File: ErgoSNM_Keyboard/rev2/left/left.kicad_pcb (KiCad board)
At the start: 2 copper layers, 115.6 x 106.7 mm, 110 parts, among them J1 USB_C_Receptacle_USB2.0, J2 USB_C_Receptacle_USB2.0, J3 PJ-393_TRRS_8P, J4 Conn_01x08, SW1 BOOT, SW2 RESET, U1 RT9013-33GB, U2 SRV05-4, U3 W25Q128JVS, U4 RP2040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

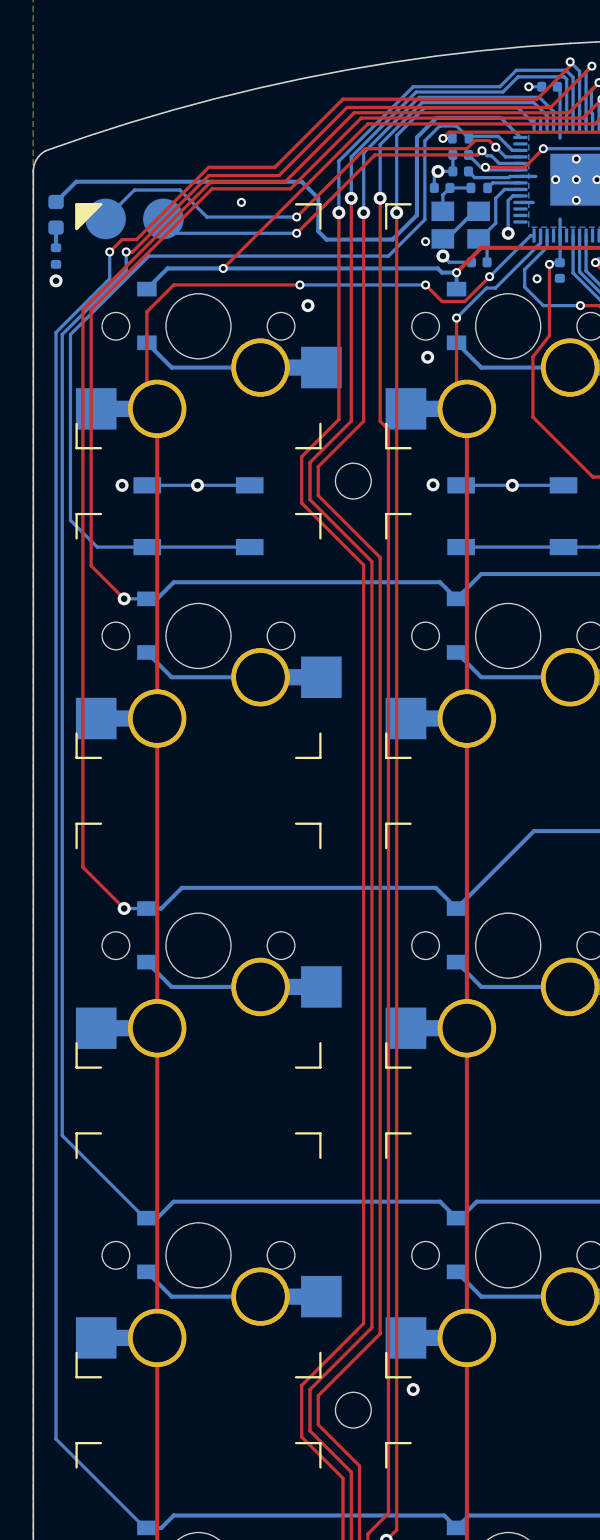
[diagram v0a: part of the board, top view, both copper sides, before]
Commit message: Add additional LED and upadrte LED position
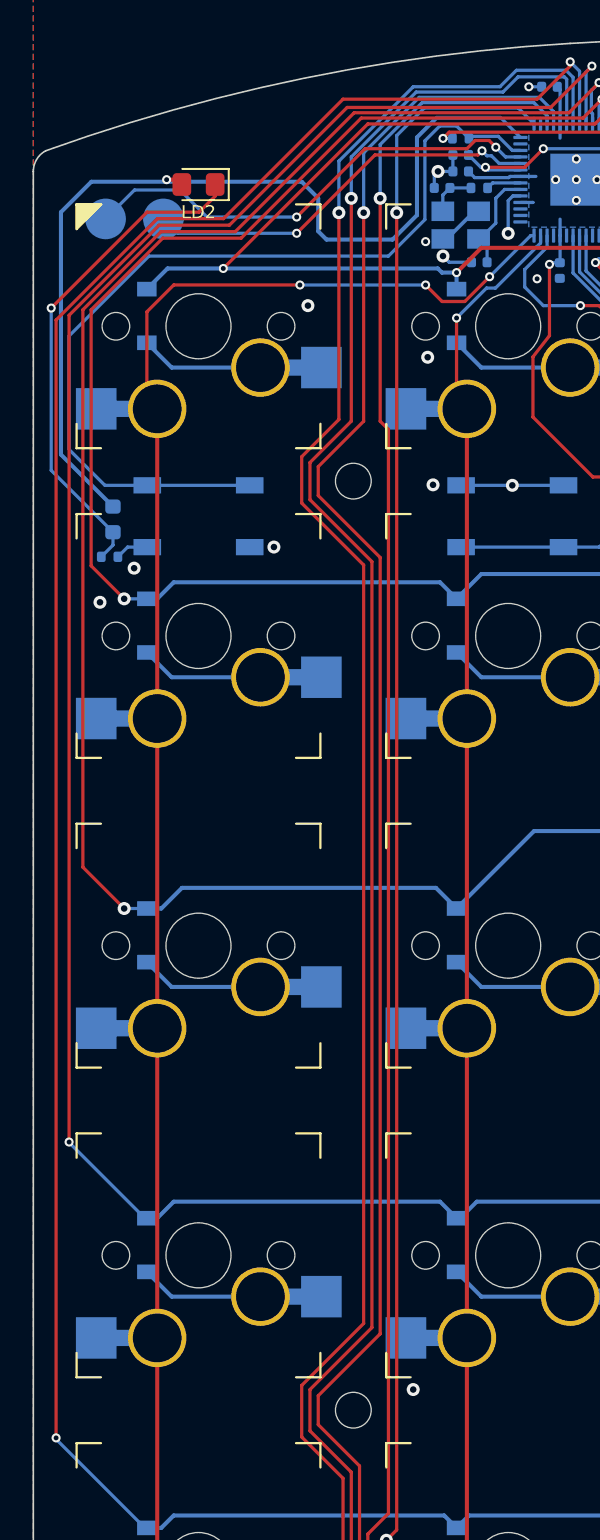
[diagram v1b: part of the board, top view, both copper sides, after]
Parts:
- added LD2: LED, LED_SMD:LED_0805_2012Metric_Pad1.15x1.40mm_HandSolder, F.Cu at (71.1, 37.0)
- moved LD1 19.1 mm to (65.9, 57.6)
- moved R3 18.8 mm to (65.7, 59.9), turned to 0 degrees
- turned SW2 to 0 degrees
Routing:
- net Net-(R3-Pad1): track 1.24 -> 30.8 mm, vias 0 -> 1
- net STATE_LED: track 38.1 -> 58.7 mm, vias 0 -> 1
- net GND: track 32.2 -> 28.0 mm, vias 58 -> 57
- net /RP2040/~{RESET}: track 59.7 -> 55.7 mm
- net ROW_3: track 202.9 -> 202.3 mm
- net ROW_4: track 220.1 -> 219.6 mm

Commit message: Update plate
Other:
- board text added: "JLCJLCJLCJLC"
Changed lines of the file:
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@@
     (fp_line (start 1 -0.6) (end -0.7 -0.6) (layer "F.Fab") (width 0.1))
     (fp_line (start -1 -0.3) (end -1 0.6) (layer "F.Fab") (width 0.1))
-    (pad "1" smd roundrect (at -1.025 0 180) (size 1.15 1.4) (layers "F.Cu" "F.Paste" "F.Mask") (roundrect_rratio 0.217391)
+    (pad "1" smd roundrect (at -1.025 0 180) (size 1.15 1.4) (layers "F.Cu" "F.Paste" "F.Mask") (roundrect_rratio 0.2173913043)
       (net 88 "Net-(R3-Pad1)") (pinfunction "K") (pintype "passive"))
-    (pad "2" smd roundrect (at 1.025 0 180) (size 1.15 1.4) (layers "F.Cu" "F.Paste" "F.Mask") (roundrect_rratio 0.217391)
+    (pad "2" smd roundrect (at 1.025 0 180) (size 1.15 1.4) (layers "F.Cu" "F.Paste" "F.Mask") (roundrect_rratio 0.2173913043)
       (net 89 "STATE_LED") (pinfunction "A") (pintype "passive"))
     (model "${KICAD6_3DMODEL_DIR}/LED_SMD.3dshapes/LED_0805_2012Metric.wrl"
@@
     (effects (font (size 1.2 1.2) (thickness 0.2)))
   )
+  (gr_text "JLCJLCJLCJLC" (at 66.802 130.81) (layer "F.SilkS")
+    (effects (font (size 1 1) (thickness 0.15)))
+  )
   (gr_text "Rev ${REVISION}" (at 74.36 97.2) (layer "B.Mask")

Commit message: Update logo
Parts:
- removed G***: LOGO, LOGO
